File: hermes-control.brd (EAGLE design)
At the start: 106 x 47 mm, 73 parts, among them J1 1981568-1, J3 2201778-1, Q2 BC849SMD, Q3 FDN360P, Q4 FDN360P, Q5 BC849SMD, Q6 MMBT3906SOT23-3, Q7 FDN360P, Q8 MMBT2222A, U1 LSM9DS1TR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

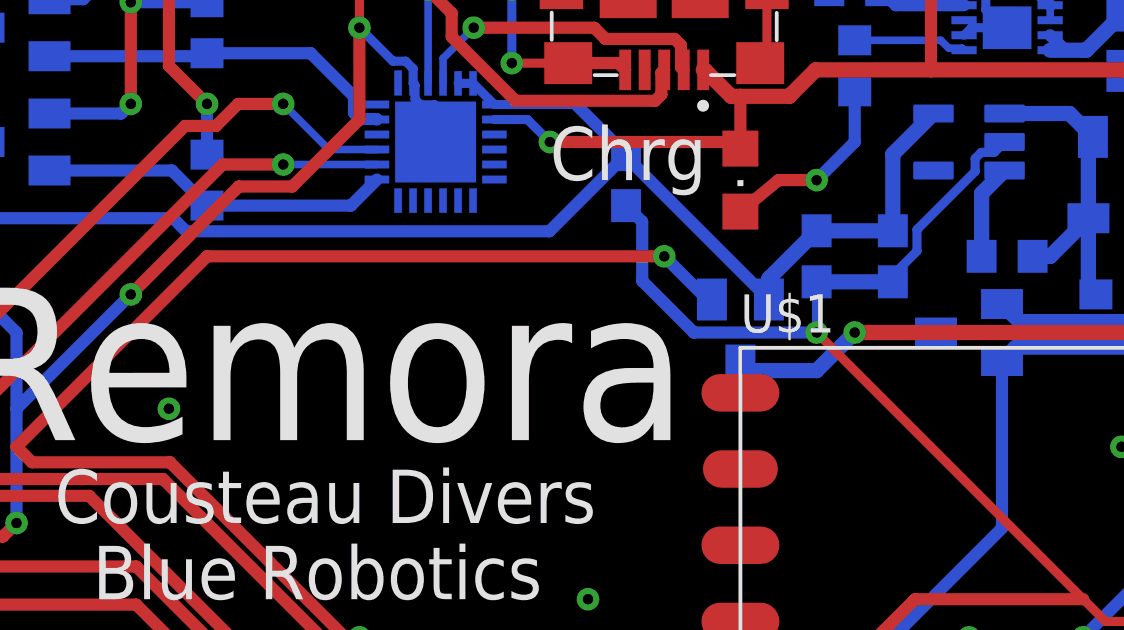
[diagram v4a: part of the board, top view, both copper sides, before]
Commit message: changed from 3.3 to vccio
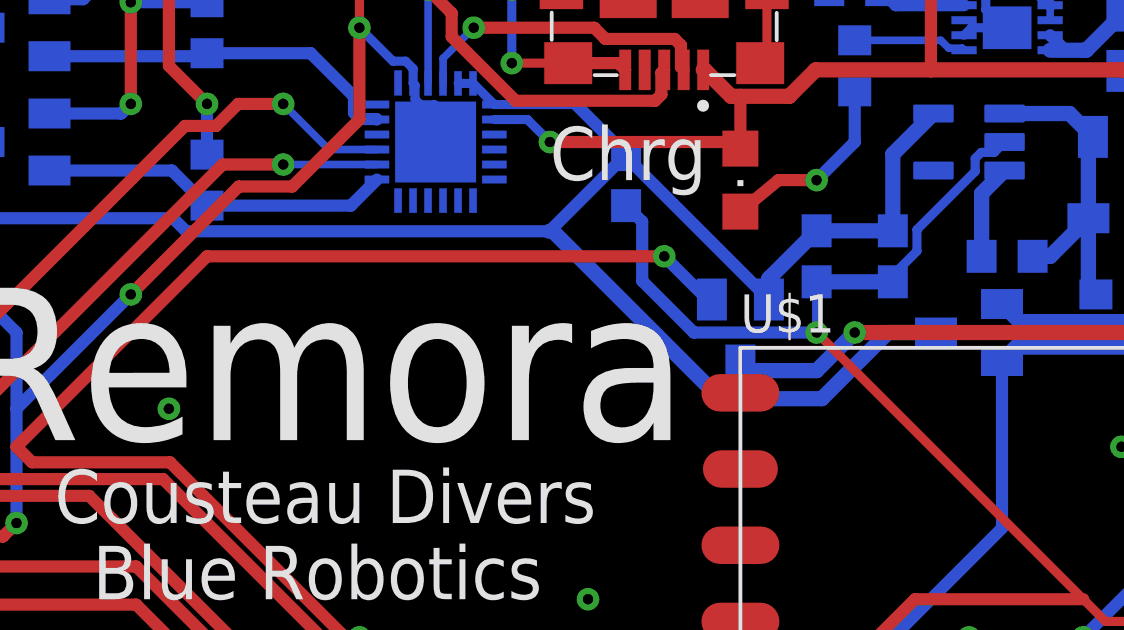
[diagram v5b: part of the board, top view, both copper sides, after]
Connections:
- net 3.3V: no longer Q8.3
- net VCCIO: now also Q8.3
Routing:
- net VCCIO: track 142.7 -> 158.8 mm
- net 3.3V: track 206.0 -> 203.3 mm
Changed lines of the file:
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@@
 <contactref element="D2" pad="1"/>
 <contactref element="S2" pad="2"/>
-<contactref element="Q8" pad="3"/>
 <wire x1="63.5" y1="3.87" x2="57.15" y2="3.87" width="0.508" layer="16"/>
 <wire x1="57.15" y1="3.87" x2="50.8" y2="3.87" width="0.508" layer="16"/>
@@
 <wire x1="71.08" y1="3.87" x2="68.58" y2="3.87" width="0.508" layer="16"/>
 <wire x1="68.58" y1="3.87" x2="63.5" y2="3.87" width="0.508" layer="16"/>
-<wire x1="72.56" y1="33.02" x2="69.85" y2="33.02" width="0.508" layer="16"/>
 <wire x1="69.85" y1="33.02" x2="68.58" y2="31.75" width="0.508" layer="16"/>
 <wire x1="68.58" y1="31.75" x2="66.3947375" y2="31.75" width="0.508" layer="16"/>
@@
 <wire x1="47.12710625" y1="36.83" x2="40.64" y2="36.83" width="0.4064" layer="16"/>
 <wire x1="47.56270625" y1="36.3944" x2="47.12710625" y2="36.83" width="0.4064" layer="16"/>
-<wire x1="59.6744" y1="36.3944" x2="47.56270625" y2="36.3944" width="0.4064" layer="16"/>
+<wire x1="47.56270625" y1="36.3944" x2="59.6744" y2="36.3944" width="0.4064" layer="16"/>
 <wire x1="62.23" y1="38.95" x2="59.6744" y2="36.3944" width="0.4064" layer="16"/>
 <wire x1="35.56" y1="16.51" x2="35.56" y2="31.75" width="0.4064" layer="16"/>
@@
 <wire x1="31.75" y1="39.37" x2="31.75" y2="41.515" width="0.4064" layer="1"/>
 <wire x1="31.75" y1="41.515" x2="31.815" y2="41.58" width="0.4064" layer="1"/>
+<contactref element="Q8" pad="3"/>
+<wire x1="65.3716625" y1="30.8136" x2="68.75319375" y2="30.8136" width="0.508" layer="16"/>
+<wire x1="59.6744" y1="36.3944" x2="59.7908625" y2="36.3944" width="0.508" layer="16"/>
+<wire x1="59.7908625" y1="36.3944" x2="65.3716625" y2="30.8136" width="0.508" layer="16"/>
+<wire x1="70.95959375" y1="33.02" x2="72.56" y2="33.02" width="0.508" layer="16"/>
+<wire x1="68.75319375" y1="30.8136" x2="70.95959375" y2="33.02" width="0.508" layer="16"/>
 </signal>
 <signal name="TX0">

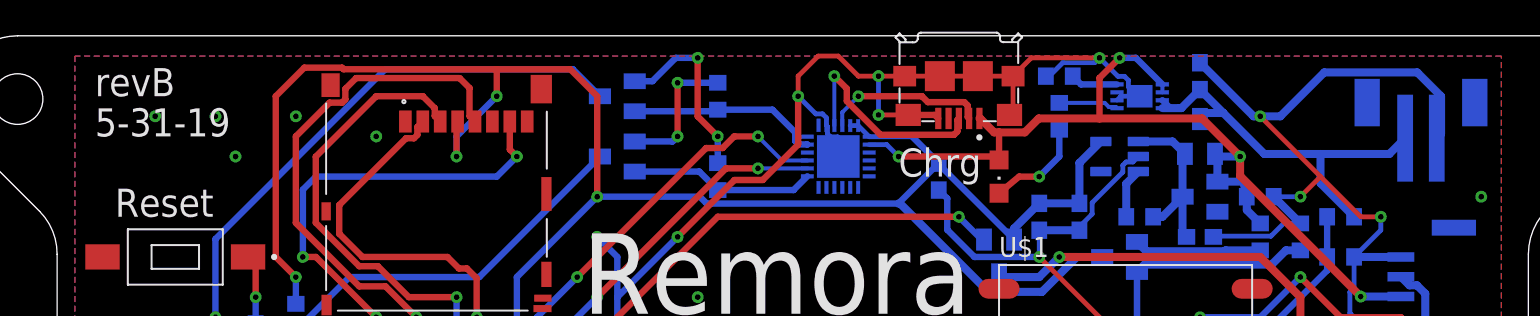
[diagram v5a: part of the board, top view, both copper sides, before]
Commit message: changed batt connection
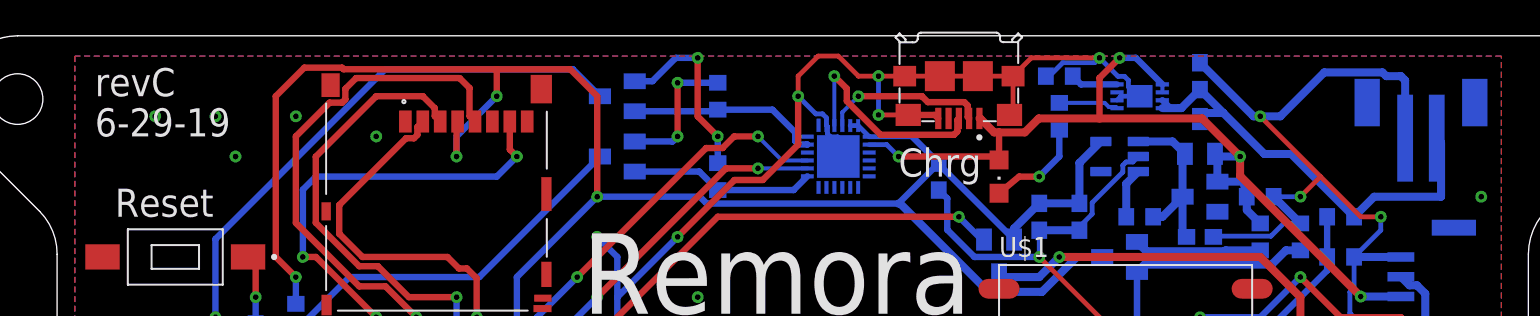
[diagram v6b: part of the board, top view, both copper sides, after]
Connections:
- net GND: now also LBAT.2; no longer LBAT.1
- net V_BATT: now also LBAT.1; no longer LBAT.2
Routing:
- net V_BATT: track 25.7 -> 28.7 mm
- net GND: track 387.6 -> 385.9 mm
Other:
- board text added: "6-29-19"
- board text added: "revC"
- board text removed: "5-31-19"
- board text removed: "revB"
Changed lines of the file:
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@@
 <text x="73.66" y="2.54" size="1.778" layer="21" rot="R90">LED3</text>
 <text x="81.28" y="2.54" size="1.778" layer="21" rot="R90">LED4</text>
-<text x="8.89" y="43.18" size="1.778" layer="21">revB</text>
-<text x="8.89" y="40.64" size="1.778" layer="21">5-31-19</text>
+<text x="8.89" y="43.18" size="1.778" layer="21">revC</text>
+<text x="8.89" y="40.64" size="1.778" layer="21">6-29-19</text>
 </plain>
 <attributes>
@@
 <contactref element="J3" pad="15"/>
 <contactref element="J3" pad="6"/>
-<contactref element="LBAT" pad="1"/>
 <contactref element="U1" pad="19"/>
 <contactref element="U1" pad="20"/>
@@
 <wire x1="82.13" y1="41.91" x2="82.55" y2="41.91" width="0.508" layer="16"/>
 <wire x1="82.55" y1="41.91" x2="83.82" y2="41.91" width="0.508" layer="16"/>
-<wire x1="86.5964" y1="44.6864" x2="92.4736" y2="44.6864" width="0.508" layer="16"/>
-<wire x1="92.4736" y1="44.6864" x2="93.98" y2="43.18" width="0.508" layer="16"/>
-<wire x1="93.98" y1="43.18" x2="93.98" y2="40.8" width="0.508" layer="16"/>
-<wire x1="93.98" y1="40.8" x2="93.71" y2="40.53" width="0.508" layer="16"/>
+<contactref element="LBAT" pad="2"/>
+<wire x1="90.2783375" y1="44.6864" x2="90.5147375" y2="44.45" width="0.508" layer="16"/>
+<wire x1="90.5147375" y1="44.45" x2="91.44" y2="44.45" width="0.508" layer="16"/>
+<wire x1="86.5964" y1="44.6864" x2="90.2783375" y2="44.6864" width="0.508" layer="16"/>
+<wire x1="91.44" y1="44.45" x2="91.71" y2="44.18" width="0.508" layer="16"/>
+<wire x1="91.71" y1="44.18" x2="91.71" y2="40.53" width="0.508" layer="16"/>
 <wire x1="83.82" y1="41.91" x2="86.5964" y2="44.6864" width="0.508" layer="16"/>
+<wire x1="91.71" y1="40.53" x2="96.52" y2="36.83" width="0" layer="19" extent="16-16"/>
+<wire x1="73.66" y1="22.86" x2="71.86" y2="24.13" width="0" layer="19" extent="1-1"/>
+<wire x1="73.495" y1="42.93" x2="74.845" y2="39.37" width="0" layer="19" extent="16-16"/>
+<wire x1="62.23" y1="17.78" x2="66.04" y2="18.31" width="0" layer="19" extent="1-1"/>
+<wire x1="37.43" y1="31.92" x2="40.64" y2="34.29" width="0" layer="19" extent="1-1"/>
+<wire x1="46.99" y1="30.48" x2="45.72" y2="34.29" width="0" layer="19" extent="1-1"/>
+<wire x1="37.43" y1="37" x2="40.64" y2="34.29" width="0" layer="19" extent="1-1"/>
+<wire x1="34.015" y1="41.58" x2="37.43" y2="37" width="0" layer="19" extent="1-1"/>
+<wire x1="37.105" y1="43.63" x2="34.015" y2="41.58" width="0" layer="19" extent="1-1"/>
+<wire x1="41.91" y1="20.32" x2="41.46" y2="26.22" width="0" layer="19" extent="1-1"/>
+<wire x1="91.44" y1="14.82" x2="91.44" y2="21.17" width="0" layer="19" extent="16-16"/>
+<wire x1="63.5" y1="7.62" x2="63.5" y2="4.03" width="0" layer="19" extent="1-16"/>
+<wire x1="63.5" y1="8.89" x2="63.5" y2="7.62" width="0" layer="19" extent="16-16"/>
+<wire x1="11.43" y1="6.35" x2="13.12" y2="5.08" width="0" layer="19" extent="16-16"/>
+<wire x1="23.53" y1="29.98" x2="24.13" y2="27.94" width="0" layer="19" extent="1-1"/>
+<wire x1="57.15" y1="10.16" x2="57.15" y2="7.62" width="0" layer="19" extent="16-16"/>
+<wire x1="8.89" y1="2.54" x2="11.9206" y2="2.29426875" width="0" layer="19" extent="16-16"/>
+<wire x1="41.91" y1="11.43" x2="38.98" y2="8.71" width="0" layer="19" extent="1-1"/>
+<wire x1="41.91" y1="13.97" x2="41.91" y2="11.43" width="0" layer="19" extent="1-1"/>
+<wire x1="19.05" y1="21.59" x2="17.78" y2="25.4" width="0" layer="19" extent="16-16"/>
+<wire x1="11.43" y1="25.4" x2="13.12" y2="20.74" width="0" layer="19" extent="1-1"/>
+<wire x1="22.86" y1="1.69" x2="17.83" y2="2.735" width="0" layer="19" extent="16-16"/>
+<wire x1="25.4" y1="1.69" x2="22.86" y2="1.69" width="0" layer="19" extent="16-16"/>
+<wire x1="27.94" y1="1.69" x2="25.4" y2="1.69" width="0" layer="19" extent="16-16"/>
+<wire x1="23.505" y1="35.905" x2="23.53" y2="29.98" width="0" layer="19" extent="1-1"/>
+<wire x1="26.67" y1="40.64" x2="23.505" y2="35.905" width="0" layer="19" extent="1-1"/>
+<wire x1="23.785" y1="43.88" x2="26.67" y2="40.64" width="0" layer="19" extent="1-1"/>
+<wire x1="21.59" y1="41.91" x2="23.785" y2="43.88" width="0" layer="19" extent="1-1"/>
+<wire x1="17.78" y1="39.37" x2="21.59" y2="41.91" width="0" layer="19" extent="1-1"/>
+<wire x1="16.51" y1="41.91" x2="17.78" y2="39.37" width="0" layer="19" extent="1-1"/>
+<wire x1="12.7" y1="41.91" x2="16.51" y2="41.91" width="0" layer="19" extent="1-1"/>
+<wire x1="60.96" y1="24.13" x2="62.23" y2="17.78" width="0" layer="19" extent="1-1"/>
+<wire x1="85.09" y1="2.54" x2="78.74" y2="4.03" width="0" layer="19" extent="1-1"/>
+<wire x1="9.37" y1="33.02" x2="11.43" y2="25.4" width="0" layer="19" extent="1-1"/>
+<wire x1="95.25" y1="5.08" x2="88.15" y2="9.95" width="0" layer="19" extent="16-16"/>
 </signal>
 <signal name="3.3V">
@@
 <contactref element="U5" pad="3"/>
 <contactref element="U5" pad="4"/>
-<contactref element="LBAT" pad="2"/>
 <contactref element="C11" pad="1"/>
 <contactref element="R23" pad="2"/>
@@
 <wire x1="77.47" y1="42.43" x2="76.865" y2="42.43" width="0.4064" layer="16"/>
 <wire x1="76.865" y1="42.43" x2="76.365" y2="42.93" width="0.4064" layer="16"/>
-<wire x1="82.81" y1="39.53" x2="85.09" y2="39.53" width="0.508" layer="16"/>
-<wire x1="86.36" y1="39.53" x2="90.71" y2="39.53" width="0.508" layer="16"/>
-<wire x1="85.09" y1="39.53" x2="86.36" y2="39.53" width="0.508" layer="16"/>
-<wire x1="90.71" y1="39.53" x2="91.71" y2="40.53" width="0.508" layer="16"/>
-<wire x1="80.22" y1="42.12" x2="82.81" y2="39.53" width="0.508" layer="16"/>
-<wire x1="88.48" y1="35.56" x2="86.36" y2="37.68" width="0.508" layer="16"/>
-<wire x1="86.36" y1="37.68" x2="86.36" y2="39.53" width="0.508" layer="16"/>
+<wire x1="82.81" y1="39.53" x2="80.22" y2="42.12" width="0.508" layer="16"/>
+<contactref element="LBAT" pad="1"/>
+<wire x1="88.48" y1="35.56" x2="89.75" y2="36.83" width="0.508" layer="16"/>
+<wire x1="89.75" y1="36.83" x2="93.98" y2="36.83" width="0.508" layer="16"/>
+<wire x1="93.98" y1="36.83" x2="93.98" y2="40.26" width="0.508" layer="16"/>
+<wire x1="93.98" y1="40.26" x2="93.71" y2="40.53" width="0.508" layer="16"/>
+<wire x1="84.51" y1="39.53" x2="82.81" y2="39.53" width="0.508" layer="16"/>
+<wire x1="88.48" y1="35.56" x2="84.51" y2="39.53" width="0.508" layer="16"/>
 </signal>
 <signal name="VCC">
